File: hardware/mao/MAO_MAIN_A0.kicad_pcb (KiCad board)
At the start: 4 copper layers, 58 x 55.4 mm, 142 parts, among them J101 USB-C, J102 BAT, J201 SERVICE, J301 LCD, J302 TOUCH TOP, J303 TOUCH REAR, J501 LRA, Q101 AO3401A, Q301 AO3400A, Q501 AO3400A, SW301 SKQGADE010, U101 TPD2E2U06, U102 BQ24073RGTR, U103 MAX17048G+T10, U104 TPS63802DLAR, U105 TPS22917DBVR, U201 ESP32-S3-WROOM-1-N8R2, U202 TCA6408ARGTR, U301 DRV5012AEDMRR, U302 DRV5012AEDMRR, U401 LSM6DSOXTR, U402 VL53L4CDV0DH/1, U403 OPT3004DNPR, U501 MAX98357AETE+T, U502 DRV2605LDGSR, U503 IRM-H638T/TR2

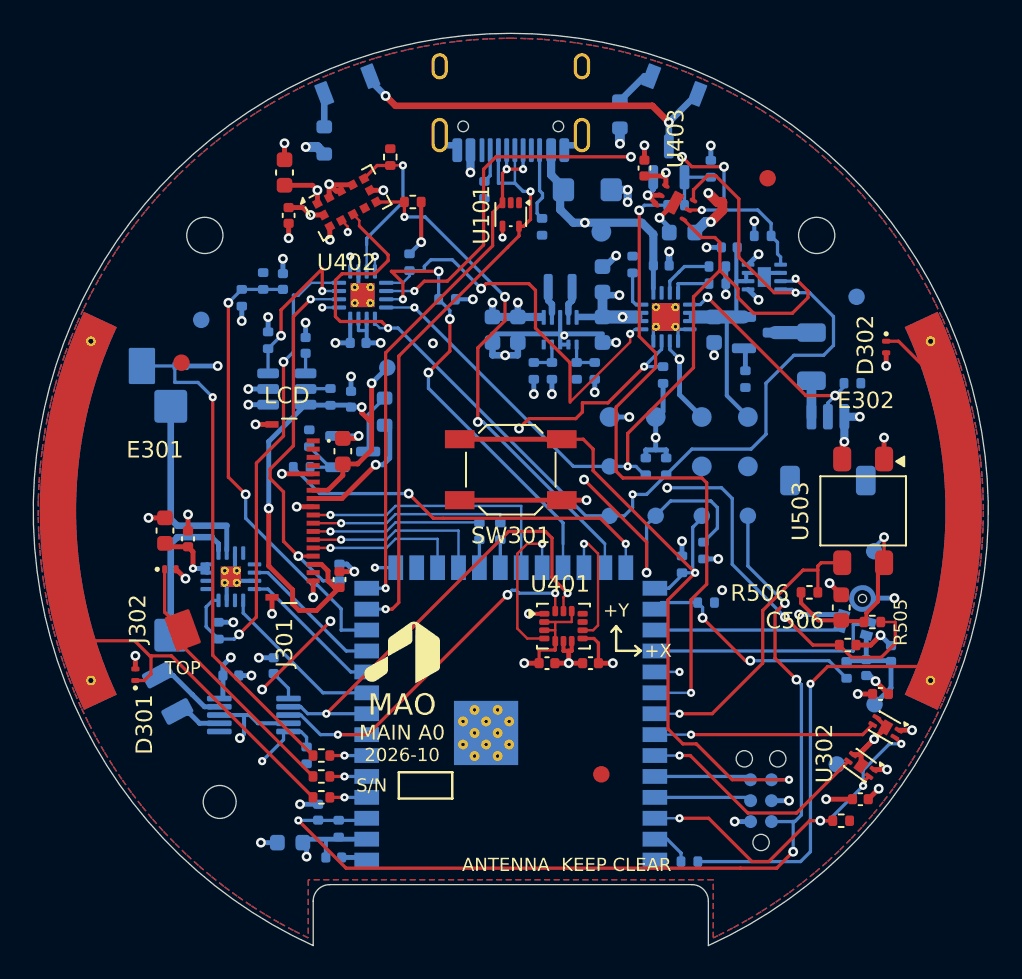
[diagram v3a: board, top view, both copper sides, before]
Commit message: MAO A0 revision: stock Winstar panel through a tail slot, AW9364 backlight, routed 4-layer board
Hardware changes from the verification audits:
- display: stock Winstar WF0128BTYAA4DNN0 (70 mm tail) through a routed slot at 9 o'clock
  to J301 on B.Cu; panel pin k on pad 19-k
- backlight: VLED+ on VSYS into an AW9364 (U303) constant-current sink, 40 mA nominal;
  Q301/R303-R305 removed
- display rail: TPS22919 (SC70-6, 1.1 mm: fits under the panel) with its VIN cap; CT cap gone
- +3V3 at 3.18 V (FB 536k), UVLO filter cap, charger ISET 4.3k (207 mA), /CE from the
  expander with a pull-down, charger moved to F under the panel, SD_MODE series 2.2k
- IR_TX on GPIO38, EXP_RST_N on GPIO39 (MTCK reset pull-up lit the IR LEDs)
- IR receiver and ToF pulled inside the ring lip; M2 boss / screw-head keep-outs

Layout: re-placed and re-routed. DRC 0 violations, 0 unconnected; every plane one piece
(the grid router now undoes any L3 route or via that splits a plane); 192 through vias.
Silk: type scale, 6 x 6 S/N field with the JLC order-number placeholder, 4.6 mm back mark,
references kept off vias, and a few easter eggs (a sleeping cat under the face, boop,
meow, 9 lives, MADE FOR BAD IDEAS).

Checks: ERC 0, silk text 0 findings, enclosure check 0 findings (mech_check.py), all
simulations pass (S3 AW9364, S10 TPS22919, S13 207 mA). Docs: bring-up, factory test,
power budget, architecture, mechanical (tail path), pin map. Firmware: dev command
"mao power charge off|on", self-test pad floor for the 3.18 V rail; merge patch regenerated.

Co-Authored-By: Claude Opus 5.5 <noreply@anthropic.com>
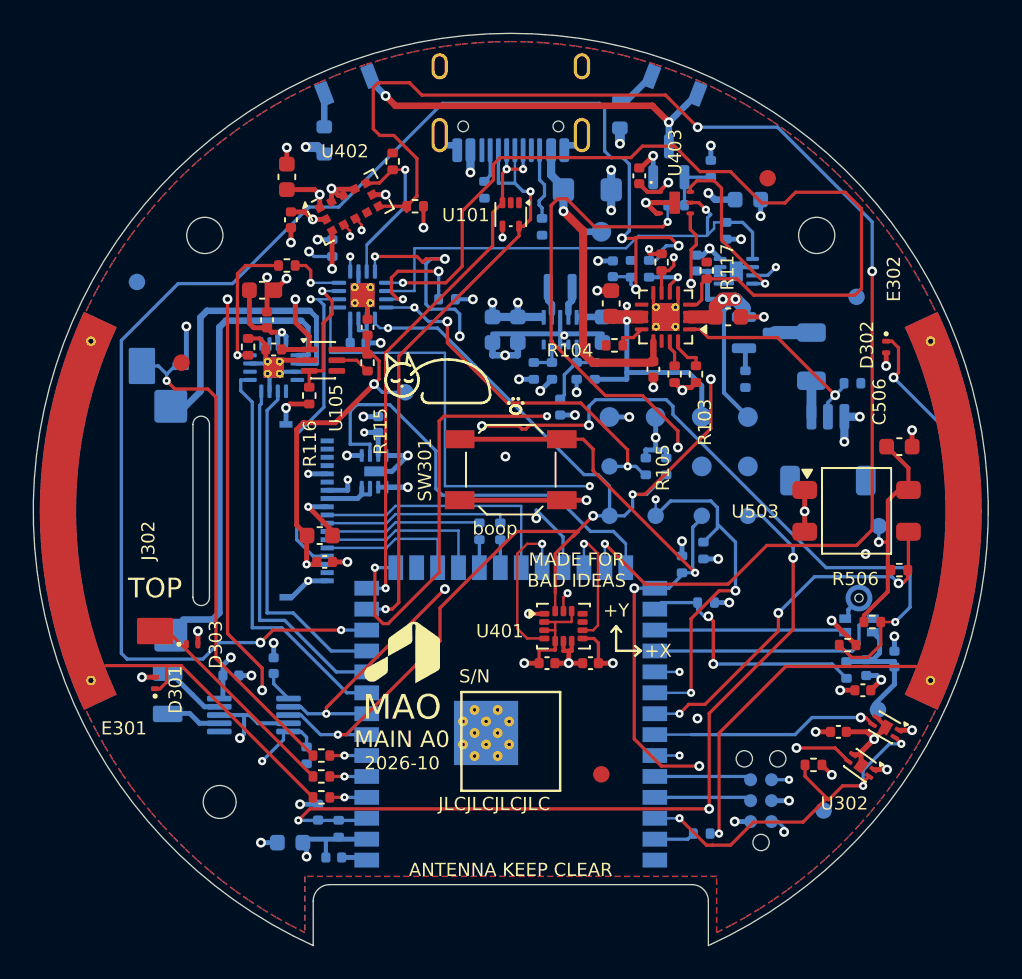
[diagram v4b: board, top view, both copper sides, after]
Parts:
- removed C108: 1nF 50V, Capacitor_SMD:C_0402_1005Metric
- removed Q301: AO3400A, Package_TO_SOT_SMD:SOT-23
- removed R107, R305: 100k, Resistor_SMD:R_0402_1005Metric
- removed R303: 10R, Resistor_SMD:R_0603_1608Metric
- removed R304: 100R, Resistor_SMD:R_0402_1005Metric
- added C110: 1uF 25V, Capacitor_SMD:C_0402_1005Metric, F.Cu at (35.6, 40.2)
- added C111: 100nF 16V, Capacitor_SMD:C_0402_1005Metric, B.Cu at (53.0, 43.7)
- added C305: 1uF 25V, Capacitor_SMD:C_0402_1005Metric, B.Cu at (42.0, 44.8)
- added R117: 100k, Resistor_SMD:R_0402_1005Metric, F.Cu at (61.9, 35.4)
- added R507: 2.2k, Resistor_SMD:R_0402_1005Metric, F.Cu at (36.4, 35.1)
- added U303: AW9364DNR, Package_DFN_QFN:DFN-8-1EP_2x2mm_P0.5mm_EP0.6x1.2mm, B.Cu at (41.7, 47.6)
- C101, C102, C103, C109, R104, R105, R106, R115, R116, R208, U102: moved to F.Cu
- J201: value SERVICE -> TAG
- J301: moved to B.Cu
- R103: value 3.0k -> 4.3k; moved to F.Cu
- R113: value 560k -> 536k
- TP13: value LCD -> LCDV
- U105: value TPS22917DBVR -> TPS22919DCKR; footprint Package_TO_SOT_SMD:SOT-23-6 -> Package_TO_SOT_SMD:SOT-363_SC-70-6; moved to F.Cu
- moved R203 24.8 mm to (58.4, 35.3)
- moved R204 22.3 mm to (57.3, 35.3)
- moved C204 20.1 mm to (56.2, 35.3)
- moved R207 19.7 mm to (39.2, 34.0)
- moved R208 17.3 mm to (34.0, 40.0)
- moved C501 15.7 mm to (34.9, 36.6), turned to 0 degrees
- moved C502 14.1 mm to (35.2, 38.4)
- moved U501 13.0 mm to (35.6, 41.3), turned to 0 degrees
- moved C506 10.4 mm to (73.6, 46.1), turned to 0 degrees
- moved R105 7.04 mm to (60.0, 41.7), turned to -90 degrees
- moved R106 6.85 mm to (59.2, 34.9), turned to 90 degrees
- moved C101 6.32 mm to (58.7, 41.4), turned to -90 degrees
- moved R103 5.65 mm to (61.2, 41.7), turned to -90 degrees
- moved R506 5.62 mm to (73.6, 53.6)
- moved C302 5.31 mm to (38.4, 51.5), turned to 0 degrees
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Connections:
- J301 pad 1: unconnected-(J301-TP_INT-Pad1) -> GND
- J301 pad 10: LCD_CS -> GND
- J301 pad 11: LCD_SCLK_P -> LCD_BL_K
- J301 pad 12: LCD_MOSI_P -> VSYS
- J301 pad 13: LCD_DC -> unconnected-(J301-TP_VDD/P6-Pad13)
- J301 pad 14: LCD_TE -> GND
- J301 pad 15: LCD_RST_N -> unconnected-(J301-TP_RST/P4-Pad15)
- J301 pad 16: 3V3_LCD -> unconnected-(J301-TP_SCL/P3-Pad16)
- J301 pad 18: GND -> unconnected-(J301-TP_INT/P1-Pad18)
- J301 pad 3: unconnected-(J301-TP_SCL-Pad3) -> 3V3_LCD
- J301 pad 4: unconnected-(J301-TP_RST-Pad4) -> LCD_RST_N
- J301 pad 5: GND -> LCD_TE
- J301 pad 6: unconnected-(J301-TP_VDD-Pad6) -> LCD_DC
- J301 pad 7: 3V3_LCD -> LCD_MOSI_P
- J301 pad 8: LCD_BL_K -> LCD_SCLK_P
- J301 pad 9: GND -> LCD_CS
- R208 pad 1: AMP_SD_N -> AMP_SD
- U102 pad 4: GND -> CHG_CE_N
- U102 pad 6: VSYS -> +3V3
- U102 pad 9: CHG_N -> unconnected-(U102-~{CHG}-Pad9)
- U105 pad 4: LCD_SW_CT -> unconnected-(U105-NC-Pad4)
- U201 pad 26: LCD_BL_PWM -> LCD_BL_CTRL
- U201 pad 31: EXP_RST_N -> IR_TX
- U201 pad 32: IR_TX -> EXP_RST_N
- U202 pad 9: CHG_N -> CHG_CE_N
- U501 pad 4: AMP_SD_N -> AMP_SD
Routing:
- net BOARD_ID: track 27.4 -> 89.8 mm, vias 2 -> 5
- net CHG_CE_N: track 0.00 -> 53.8 mm, vias 0 -> 1
- net TOF_INT_N: track 30.6 -> 83.1 mm
- net LCD_BL_CTRL: track 0.00 -> 26.4 mm
- net AMP_SD_N: track 29.4 -> 3.36 mm, vias 2 -> 1
- net CHG_N: track 25.0 -> 0.00 mm, vias 2 -> 0
- net LCD_BL_PWM: track 22.9 -> 0.00 mm, vias 2 -> 0
- net GND: track 112.7 -> 131.5 mm, vias 63 -> 61
- net SPK_P: track 9.18 -> 27.8 mm
- net AMP_DIN: track 9.46 -> 23.8 mm
- net AMP_BCLK: track 8.24 -> 21.1 mm
- net AMP_LRCLK: track 8.13 -> 20.1 mm
- net 3V3_LCD: track 34.7 -> 23.8 mm, vias 3 -> 2
- net IR_RX_PWR: track 48.6 -> 59.5 mm, vias 3 -> 6
- net VSYS: track 25.1 -> 35.6 mm, vias 10 -> 9
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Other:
- outline, holes or cut-outs redrawn
- board text added: "9 lives"
- board text added: "JLCJLCJLCJLC"
- board text added: "LCDV"
- board text added: "MADE FOR BAD IDEAS"
- board text added: "MAO A0"
- board text added: "TAG"
- board text added: "boop"
- board text added: "meow"
- board text removed: "MAO MAIN A0"
- board text removed: "SERVICE"

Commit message: MAO A0 audit 2: module inside the outline, designed corners, tab keep-outs, legible silk and assembly drawing
Second ODD JOBS and electrical audits of the revised board (fixes; the documents follow separately):

- X1: the ESP32-S3 module's antenna-end corners reached r 30.08 mm, past the 29 mm board and into the
  enclosure wall. The module moves 1.25 mm inward (corners r 28.89, 1.1 mm to the wall), the notch and
  antenna keep-out with it, the cell datum 0.6 mm towards 12 o'clock (12 mm to the antenna again).
  mech_check.py now tests every body against the wall.
- The designed copper at the module follows it; the display bus is redesigned (five nested lanes drop to
  J301 west of the module corner), the backlight driver moves up 1.25 mm, the I2S, I2C, touch and PDM
  lanes re-angle so their far ends stay put, and the service field takes a 2.8 mm grid.
- X4: the router costs L3 tracks under (and B tracks over) other nets' copper.
- X5: the board-ID divider moves onto F at GPIO8 (the only ADC line is ~3 mm, was 89.8 mm).
- IR_TX runs one L3 lane down the empty east half; the three expander lines that fight for the
  north-west corner keep the paths the router found together.
- W-e: fixed breakaway-tab spots with copper keep-outs (1.55 mm on every layer).
- W-i, N-12: VSYS leaves the charger through two 0.6/0.3 mm vias; amplifier VDD via 0.6/0.3; module
  3V3 feed 0.5 mm with two plane vias.
- GND fence (ring + coverage vias) and decoupling-cap vias after routing, with a plane-neck check;
  the router's plane model erodes region outlines by a grid cell; via clearance repair after routing.
- Silk: footprint outlines printed at 0.15 mm; back identity 1.3 mm over the mark; field names 0.8 mm
  with via-free spots; eggs keep off reference room; references with leaders where no spot beside the
  part exists (46 of 54 on silk).
- Assembly drawing redrawn (A3 per side at 4.5:1, every reference legible, no pad numbers).

DRC 0 / 0 unconnected / parity 0, planes one piece eac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
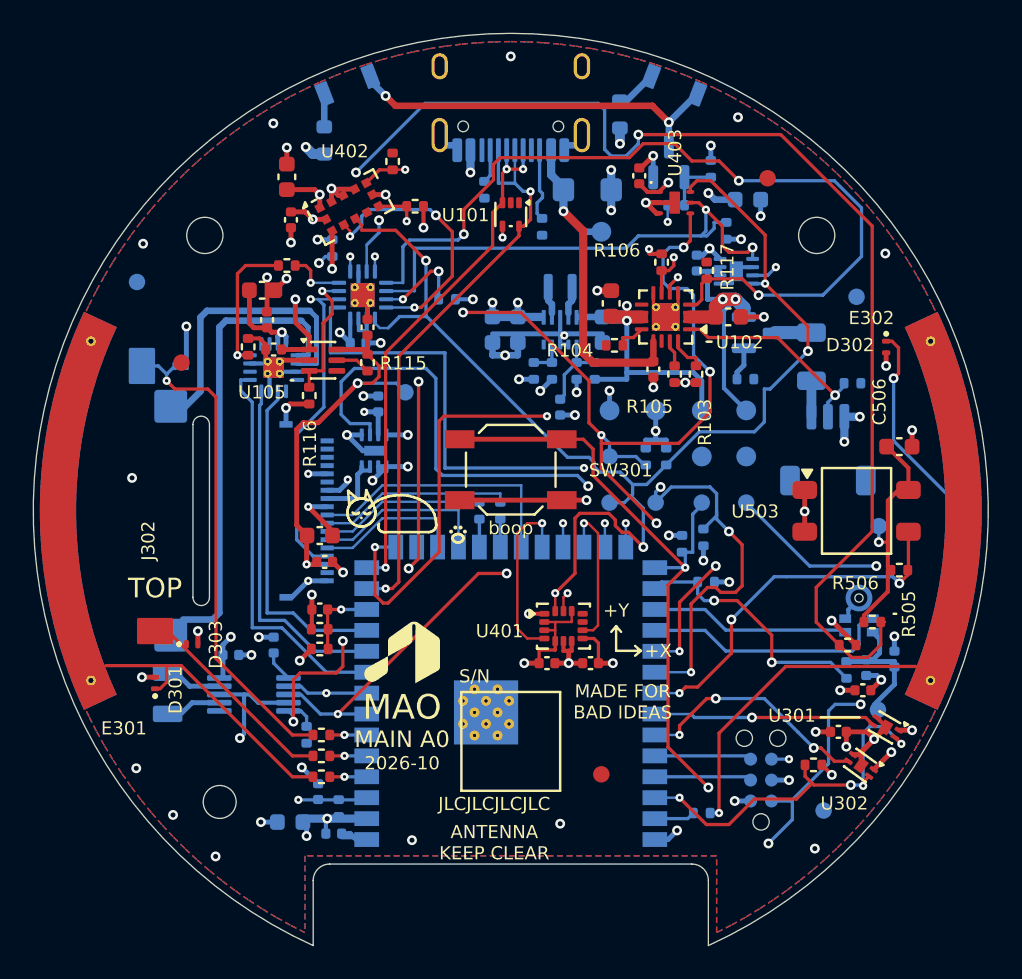
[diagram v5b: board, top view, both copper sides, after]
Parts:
- C204, R203, R204: moved to F.Cu
- moved R203 30.5 mm to (38.4, 58.4), turned to 0 degrees
- moved R204 28.9 mm to (38.4, 57.2), turned to 180 degrees
- moved C204 27.3 mm to (38.4, 56.0), turned to 180 degrees
- moved C202 1.45 mm to (39.2, 69.6)
- moved C201 1.25 mm to (36.6, 68.9)
- moved C203 1.25 mm to (38.3, 67.0)
- moved C305 1.25 mm to (42.0, 43.5)
- moved C503 1.25 mm to (33.0, 58.8)
- moved C504 1.25 mm to (35.6, 58.1)
- moved J201 1.25 mm to (65.2, 66.3)
- moved R201 1.25 mm to (39.5, 68.0)
- moved R202 1.25 mm to (60.4, 52.0)
- moved R301 1.25 mm to (49.4, 50.0)
- moved R302 1.25 mm to (48.1, 50.0)
- moved R307 1.25 mm to (38.5, 66.2)
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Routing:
- net BOARD_ID: track 89.8 -> 4.12 mm, vias 5 -> 1
- net TOF_INT_N: track 83.1 -> 36.4 mm, vias 3 -> 2
- net IR_RX_PWR: track 59.5 -> 78.0 mm, vias 6 -> 3
- net I2C_SCL: track 94.0 -> 104.4 mm, vias 9 -> 11
- net MCU_EN: track 57.2 -> 66.5 mm
- net GND: track 131.5 -> 138.5 mm, vias 61 -> 74
- net IR_TX: track 44.1 -> 38.3 mm
- net I2C_SDA: track 93.9 -> 98.7 mm
- net LCD_RST_N: track 26.2 -> 31.0 mm
- net EXP_INT_N: track 28.8 -> 24.3 mm
- net HAPTIC_EN: track 44.8 -> 40.5 mm, vias 4 -> 5
- net LCD_BL_CTRL: track 26.4 -> 30.5 mm, vias 0 -> 2
- net SENSE_ALRT_N: track 30.3 -> 32.2 mm, vias 1 -> 2
- net HALL_B: track 12.1 -> 13.9 mm, vias 2 -> 3
- net TOF_XSHUT: track 9.69 -> 11.1 mm, vias 1 -> 2
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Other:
- outline, holes or cut-outs redrawn
